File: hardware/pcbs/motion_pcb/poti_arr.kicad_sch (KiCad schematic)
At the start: 0 parts

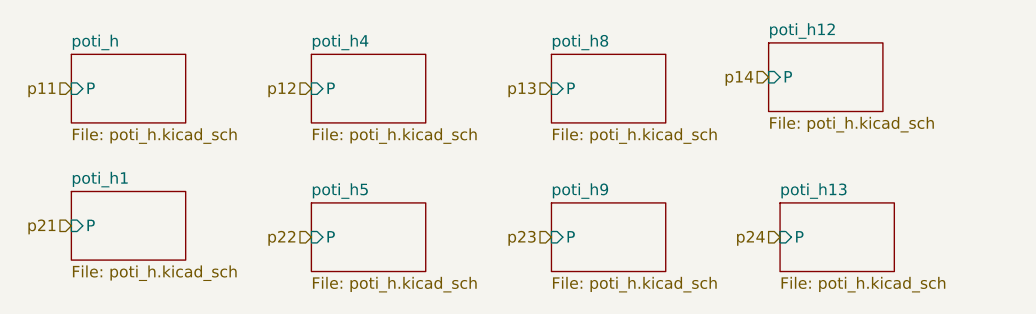
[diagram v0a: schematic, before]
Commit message: created submodule for enc pot mix
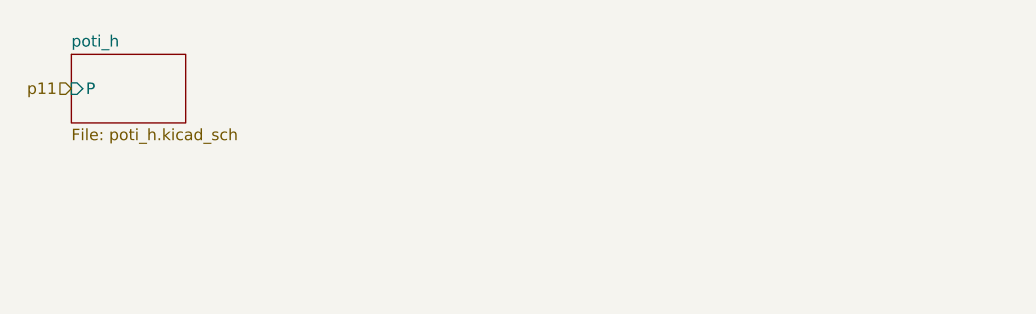
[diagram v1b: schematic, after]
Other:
- removed sheet poti_h1
- removed sheet poti_h12
- removed sheet poti_h13
- removed sheet poti_h4
- removed sheet poti_h5
- removed sheet poti_h8
- removed sheet poti_h9

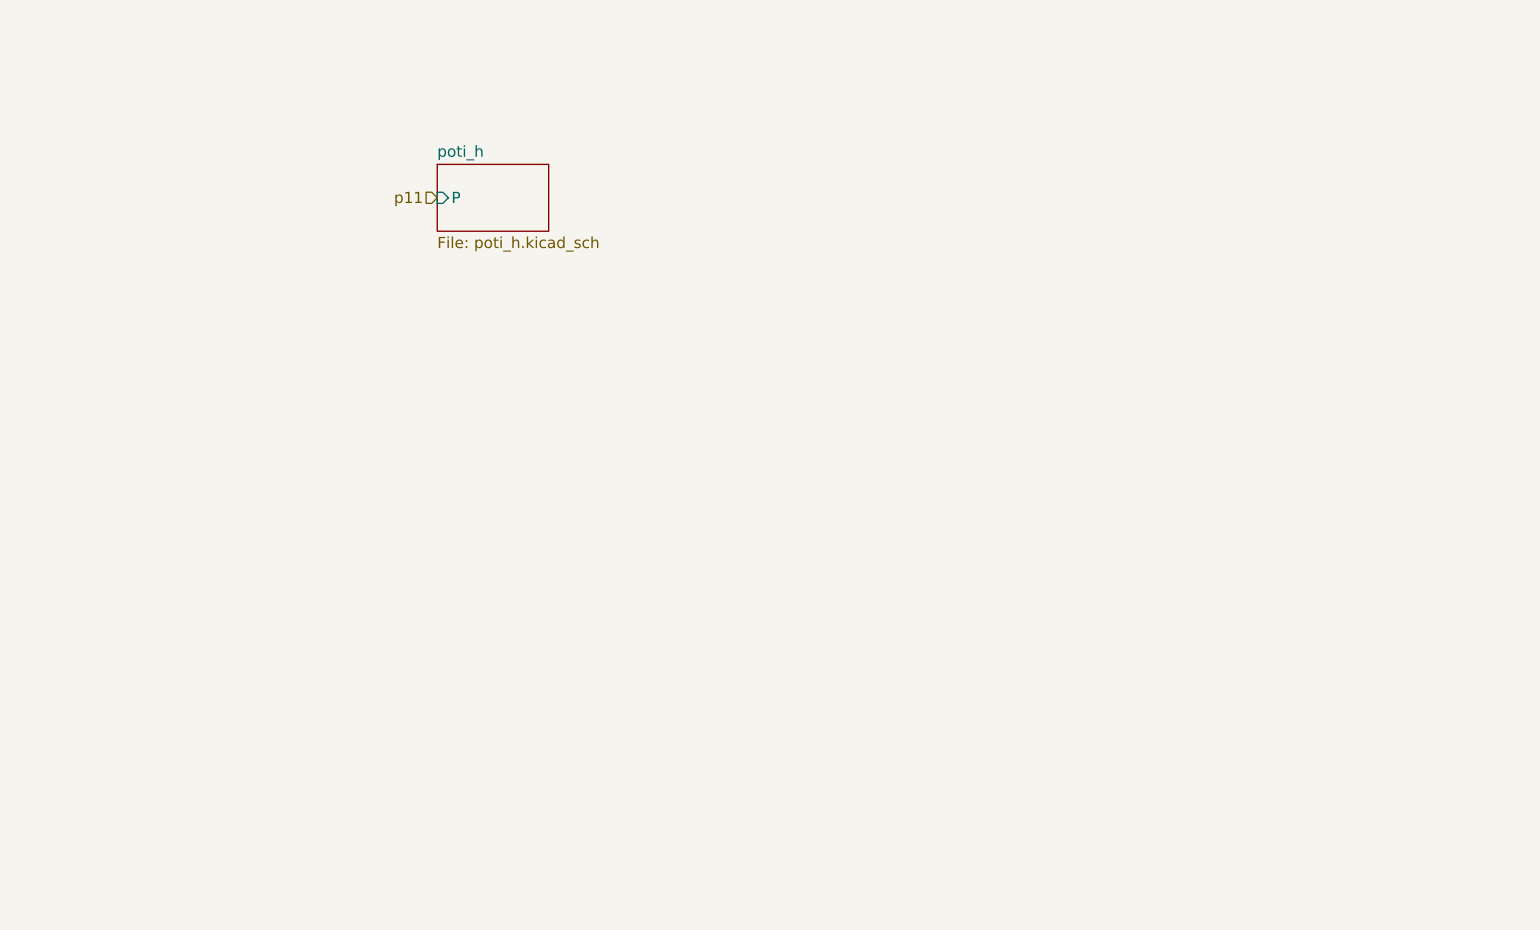
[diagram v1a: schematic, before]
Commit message: changing labels
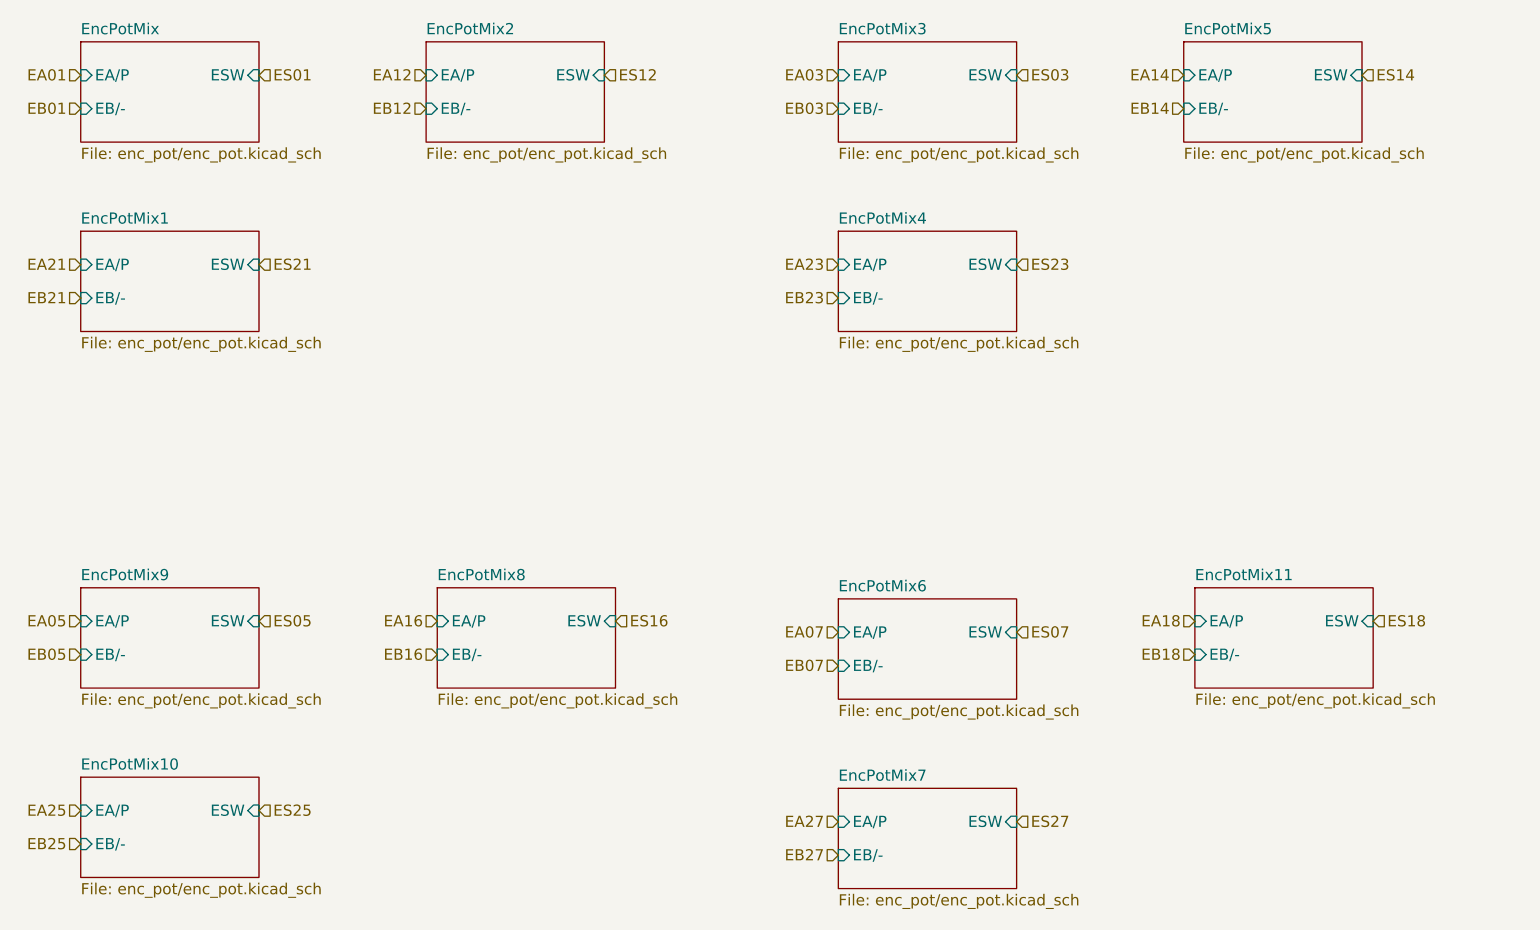
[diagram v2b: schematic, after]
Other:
- removed sheet poti_h
- added sheet EncPotMix (enc_pot/enc_pot.kicad_sch)
- added sheet EncPotMix1 (enc_pot/enc_pot.kicad_sch)
- added sheet EncPotMix10 (enc_pot/enc_pot.kicad_sch)
- added sheet EncPotMix11 (enc_pot/enc_pot.kicad_sch)
- added sheet EncPotMix2 (enc_pot/enc_pot.kicad_sch)
- added sheet EncPotMix3 (enc_pot/enc_pot.kicad_sch)
- added sheet EncPotMix4 (enc_pot/enc_pot.kicad_sch)
- added sheet EncPotMix5 (enc_pot/enc_pot.kicad_sch)
- added sheet EncPotMix6 (enc_pot/enc_pot.kicad_sch)
- added sheet EncPotMix7 (enc_pot/enc_pot.kicad_sch)
- added sheet EncPotMix8 (enc_pot/enc_pot.kicad_sch)
- added sheet EncPotMix9 (enc_pot/enc_pot.kicad_sch)
